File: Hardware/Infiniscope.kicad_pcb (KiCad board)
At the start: 2 copper layers, 60 x 40 mm, 30 parts, among them J1 USB_C_Receptacle_USB2.0_16P, J2 Conn_Coaxial, J4 5051101297, SW1 SW_Push, U1 RP2350A, U2 MCP1700x-330xxTT, U3 W25Q128JVP, U4 AD9238BSTRL-65, U5 OPA2320AIDGKR, U6 REF5025ID, U7 TLV3502AIDR, Y1 Crystal_GND24, Y2 10 mhz cmos oscillator

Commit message: updated pcb
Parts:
- removed C13: 100n, Capacitor_SMD:C_0402_1005Metric
- added C14: 100n, Capacitor_SMD:C_0402_1005Metric, F.Cu at (141.2, 81.4)
- added R4: 10K, Resistor_SMD:R_0402_1005Metric, F.Cu at (160.6, 94.2)
- added R5: 10K, Resistor_SMD:R_0402_1005Metric, F.Cu at (136.9, 105.5)
- added R6: 10K, Resistor_SMD:R_0402_1005Metric, F.Cu at (145.0, 105.5)
- added R7: 10K, Resistor_SMD:R_0402_1005Metric, F.Cu at (153.0, 105.5)
- added R8: 10K, Resistor_SMD:R_0402_1005Metric, F.Cu at (145.0, 111.5)
- added R9: 10K, Resistor_SMD:R_0402_1005Metric, F.Cu at (145.0, 99.5)
- added SW2: SW_Push, Button_Switch_SMD:SW_SPST_PTS810, F.Cu at (159.0, 96.5)
- added SW3: SW_Push, Button_Switch_SMD:SW_SPST_PTS810, F.Cu at (135.5, 107.9)
- added SW4: SW_Push, Button_Switch_SMD:SW_SPST_PTS810, F.Cu at (143.5, 107.9)
- added SW5: SW_Push, Button_Switch_SMD:SW_SPST_PTS810, F.Cu at (151.5, 107.9)
- added SW6: SW_Push, Button_Switch_SMD:SW_SPST_PTS810, F.Cu at (143.5, 101.9)
- added SW7: SW_Push, Button_Switch_SMD:SW_SPST_PTS810, F.Cu at (143.5, 113.9)
- Y1: footprint Crystal:Crystal_SMD_0603-4Pin_6.0x3.5mm -> Crystal:Crystal_SMD_3225-4Pin_3.2x2.5mm
- moved C11 75.4 mm to (137.4, 88.3), turned to 180 degrees
- moved Y1 72.9 mm to (136.1, 86.1), turned to 180 degrees
- moved C8 72.3 mm to (137.4, 89.3), turned to 180 degrees
- moved C1 71.4 mm to (135.5, 88.3)
- moved C2 70.2 mm to (136.6, 83.9), turned to 180 degrees
- moved C10 66.9 mm to (142.7, 91.4), turned to -90 degrees
- moved Y2 66.1 mm to (131.2, 68.2), turned to -90 degrees
- moved C12 65.2 mm to (147.4, 87.6)
- moved U6 64.2 mm to (134.5, 63.1)
- moved C7 63.8 mm to (146.0, 81.8), turned to 90 degrees
- moved C9 62.6 mm to (147.1, 90.3)
- moved C6 62.3 mm to (147.4, 85.8)
- moved C5 62.0 mm to (144.8, 91.4), turned to -90 degrees
- moved C4 61.2 mm to (145.7, 91.4), turned to -90 degrees
- moved U3 60.2 mm to (149.3, 80.7), turned to -90 degrees
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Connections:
- U1 pad 29: unconnected-(U1-GPIO18-Pad29) -> /BTN_BACK
- U1 pad 31: unconnected-(U1-GPIO19-Pad31) -> /BTN_DOWN
- U1 pad 32: unconnected-(U1-GPIO20-Pad32) -> /BTN_MENU
- U1 pad 33: unconnected-(U1-GPIO21-Pad33) -> /BTN_UP
- U1 pad 34: unconnected-(U1-GPIO22-Pad34) -> /BTN_RUN
- U1 pad 35: unconnected-(U1-GPIO23-Pad35) -> /BTN_PWR
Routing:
- net /BTN_DOWN: track 0.00 -> 29.7 mm
- net /BTN_RUN: track 0.00 -> 27.3 mm
- net /BTN_BACK: track 0.00 -> 25.2 mm, vias 0 -> 2
- net /BTN_PWR: track 0.00 -> 24.3 mm
- net /BTN_MENU: track 0.00 -> 23.6 mm
- net /IN1+: track 0.00 -> 19.6 mm
- net /BTN_UP: track 0.00 -> 17.2 mm
- net /SDA: track 16.7 -> 0.00 mm
- net /RESET: track 16.6 -> 0.00 mm
- net /D/C: track 15.7 -> 0.00 mm
- net /CS: track 15.6 -> 0.00 mm
- net /SCL: track 15.6 -> 0.00 mm
- net +3V3: track 0.50 -> 12.9 mm, vias 0 -> 8
- net /DATA+: track 10.8 -> 0.00 mm
- net /DATA-: track 10.0 -> 0.00 mm
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- added copper zone on B.Cu, net +3V3
- added copper zone on In2.Cu, net +3V3
- added copper zone on In1.Cu, net GND
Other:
- board size 60 x 40 mm -> 40 x 60 mm
- copper layers 2 -> 4

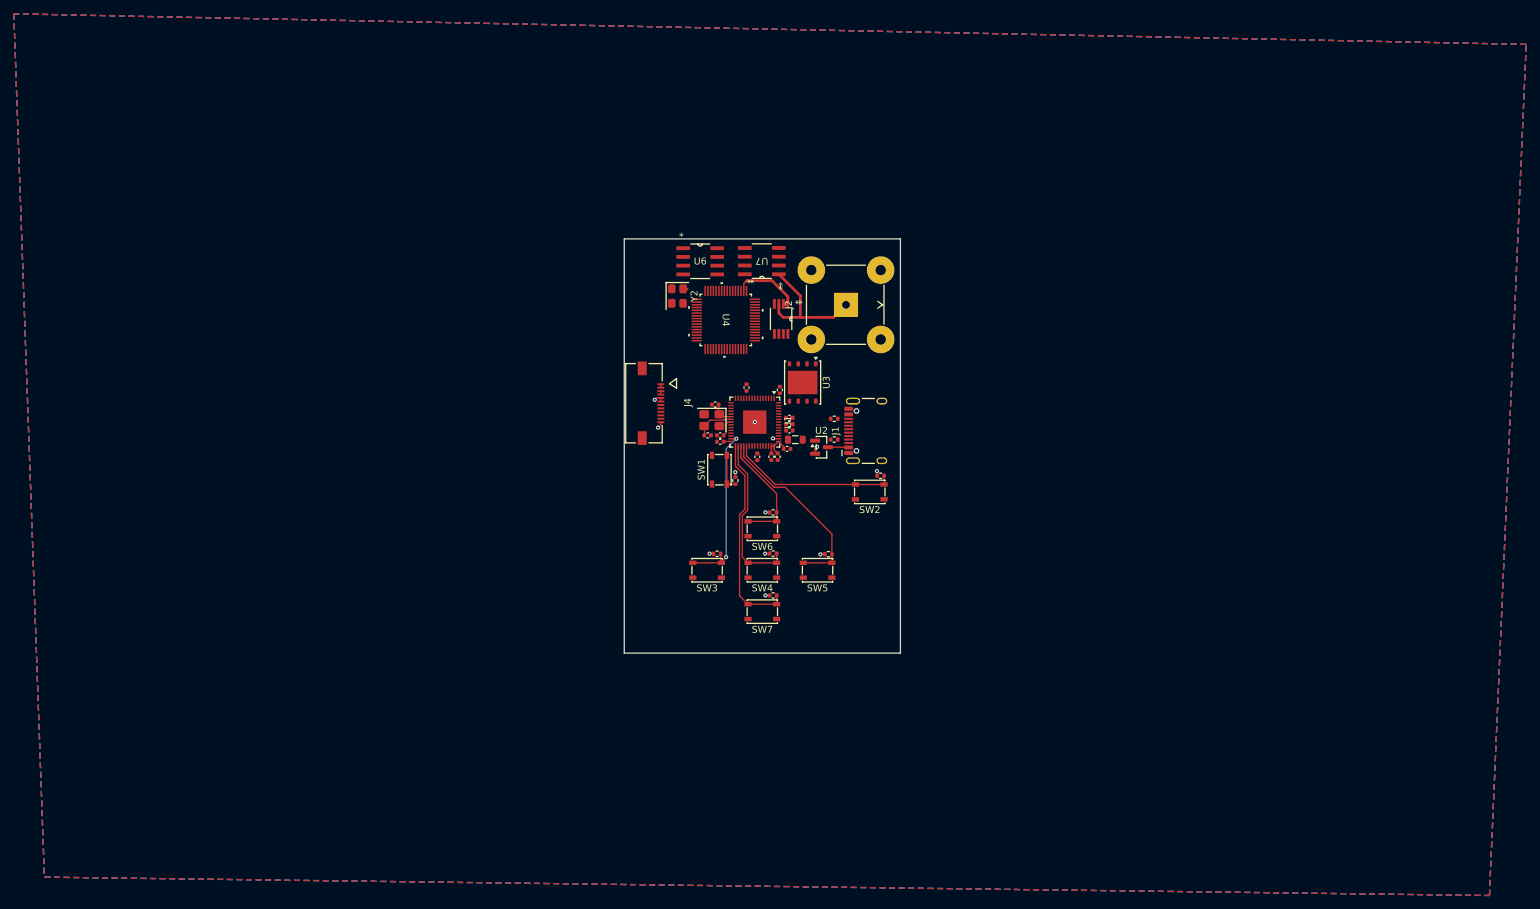
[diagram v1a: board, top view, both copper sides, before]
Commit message: added mounting holes
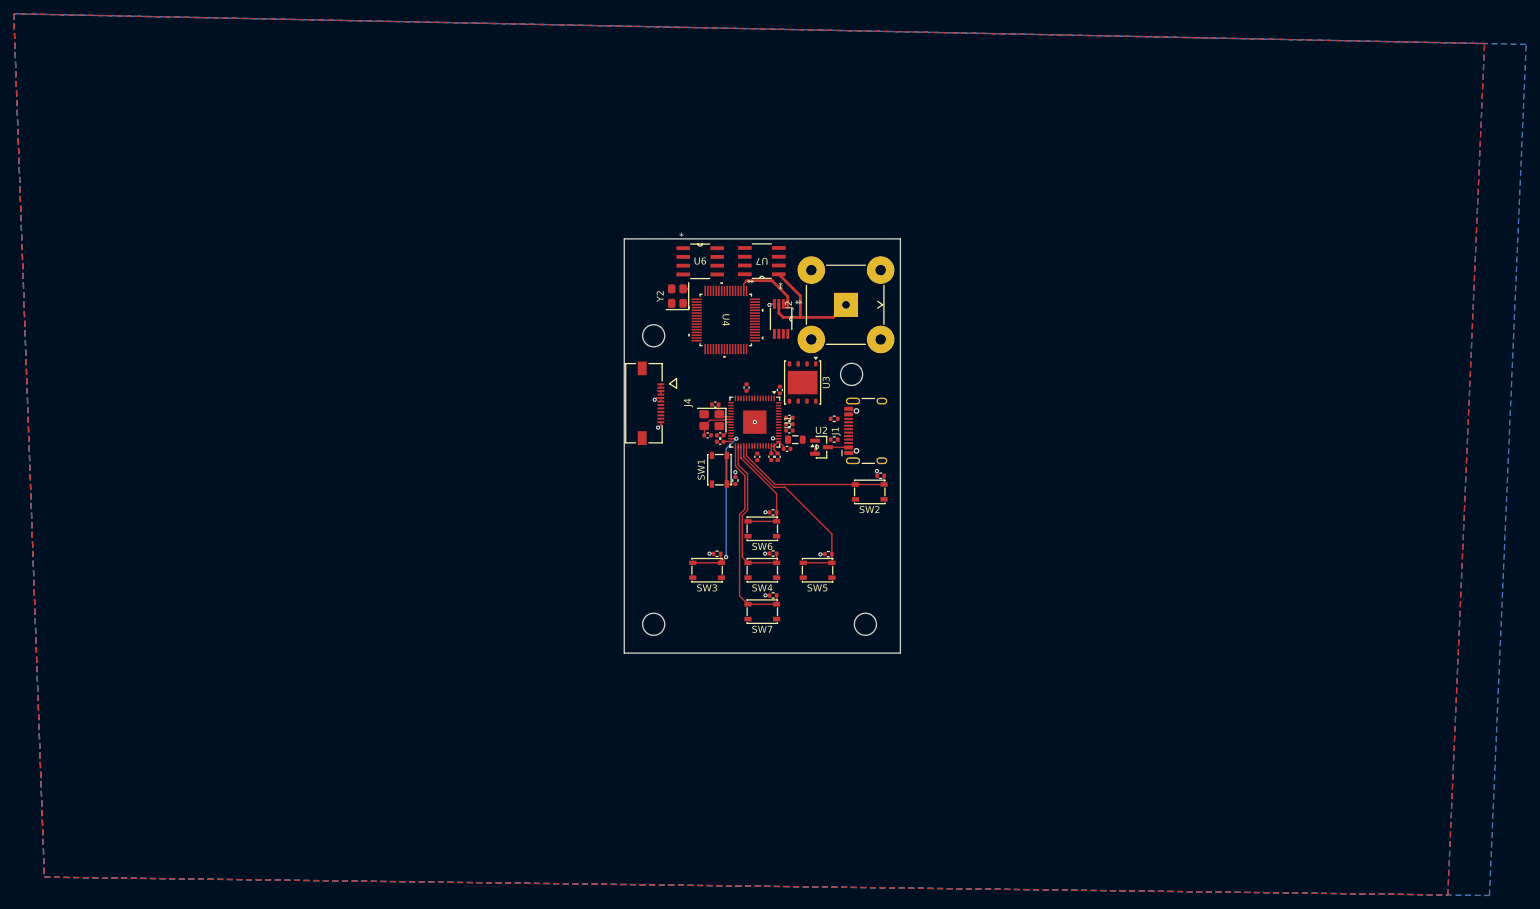
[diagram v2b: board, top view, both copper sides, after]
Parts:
- added H1: MountingHole, MountingHole:MountingHole_3.2mm_M3, B.Cu at (156.4, 79.5)
- added H2: MountingHole, MountingHole:MountingHole_3.2mm_M3, B.Cu at (158.4, 115.7)
- added H3: MountingHole, MountingHole:MountingHole_3.2mm_M3, B.Cu at (127.7, 115.7)
- added H4: MountingHole, MountingHole:MountingHole_3.2mm_M3, B.Cu at (127.7, 73.9)
- turned Y2 to 90 degrees
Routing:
- net GND: track 3.78 -> 5.13 mm, vias 4 -> 5
- net +3V3: track 12.9 -> 12.3 mm

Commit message: Completed PCB
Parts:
- moved C14 1.11 mm to (141.4, 80.3)
- moved C11 0.25 mm to (137.4, 88.6)
- moved C8 0.25 mm to (137.4, 89.5)
- moved L1 0.10 mm to (148.2, 89.1)
- moved C9 0.10 mm to (147.1, 90.4)
- moved C6 0.07 mm to (147.4, 85.7)
- moved C12 0.07 mm to (147.4, 87.6)
- moved C3 0.07 mm to (147.4, 86.6)
- moved Y1 0.06 mm to (136.1, 86.1)
- renumbered SW3 to BACK, SW7 to DOWN, SW4 to MENU, SW2 to PWR, SW5 to RUN, SW6 to UP
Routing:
- net +3V3: track 12.3 -> 47.0 mm, vias 8 -> 29
- net +1V1: track 2.64 -> 31.0 mm, vias 0 -> 4
- net /GP12: track 0.00 -> 22.0 mm, vias 0 -> 2
- net /SDA: track 0.00 -> 14.8 mm, vias 0 -> 2
- net /DATA+: track 0.00 -> 14.7 mm, vias 0 -> 2
- net /RESET: track 0.00 -> 14.7 mm, vias 0 -> 2
- net /DATA-: track 0.00 -> 14.4 mm, vias 0 -> 2
- net /ADC_CLK: track 0.00 -> 13.4 mm
- net /GP1: track 0.00 -> 12.9 mm
- net /SCL: track 0.00 -> 12.6 mm, vias 0 -> 2
- net /CS: track 0.00 -> 12.5 mm, vias 0 -> 2
- net /GP2: track 0.00 -> 12.4 mm
- net GND: track 5.13 -> 16.9 mm, vias 5 -> 12
- net /GP3: track 0.00 -> 11.8 mm
- net /GP5: track 0.00 -> 11.2 mm, vias 0 -> 2
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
